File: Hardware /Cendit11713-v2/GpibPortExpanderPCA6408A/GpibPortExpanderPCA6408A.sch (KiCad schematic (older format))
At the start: 2 parts

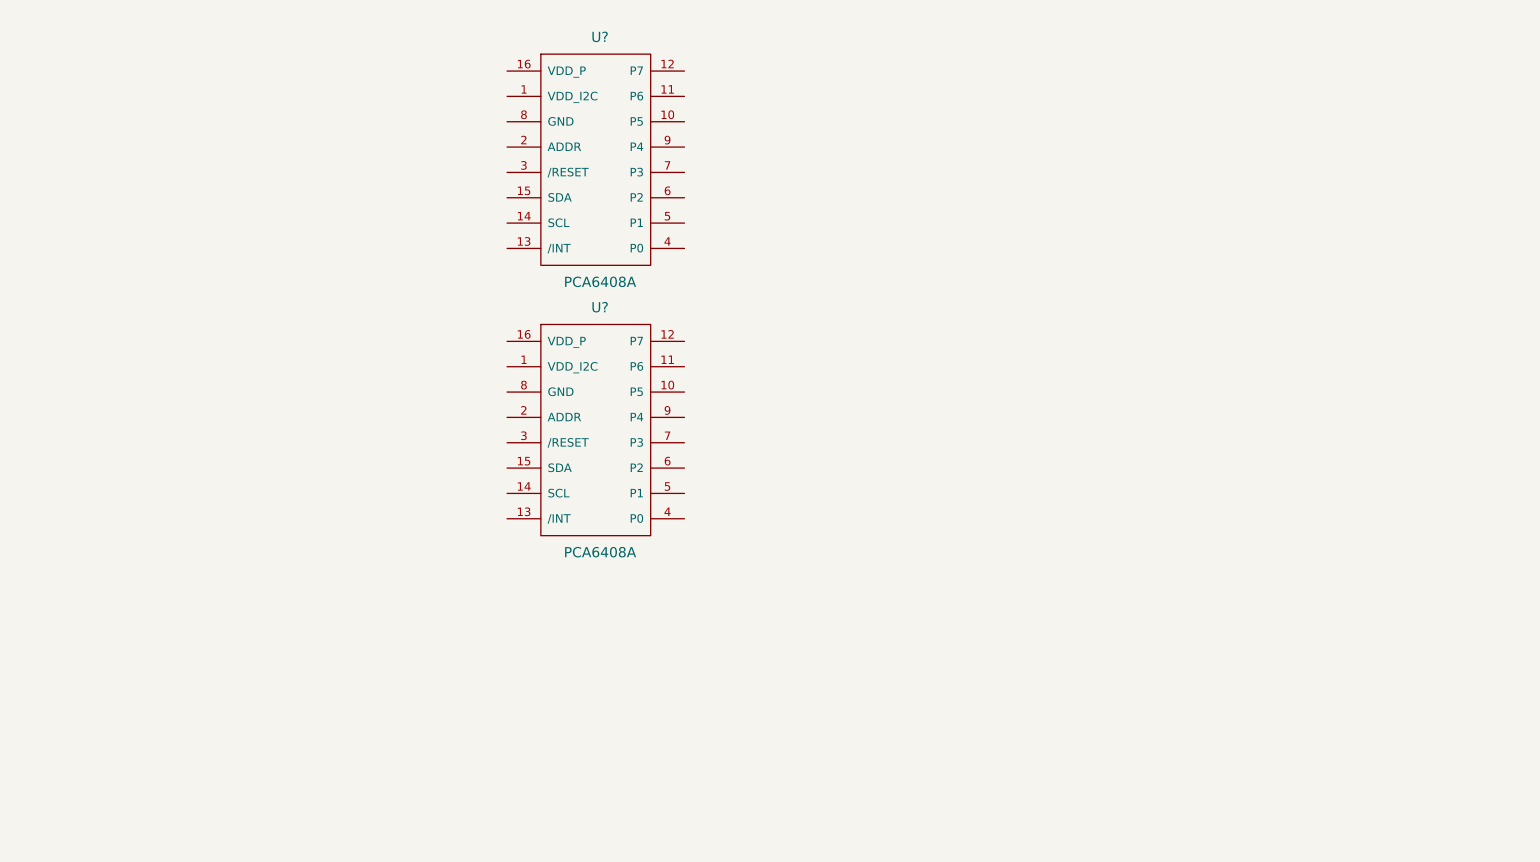
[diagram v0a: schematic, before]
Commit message: Trabajo en CenditLab.Reducido + Cendit11713
  - CenditLab componenets GUI setup frecuencia
  - Cendit11713 esquematicos expansor puerto GPIB
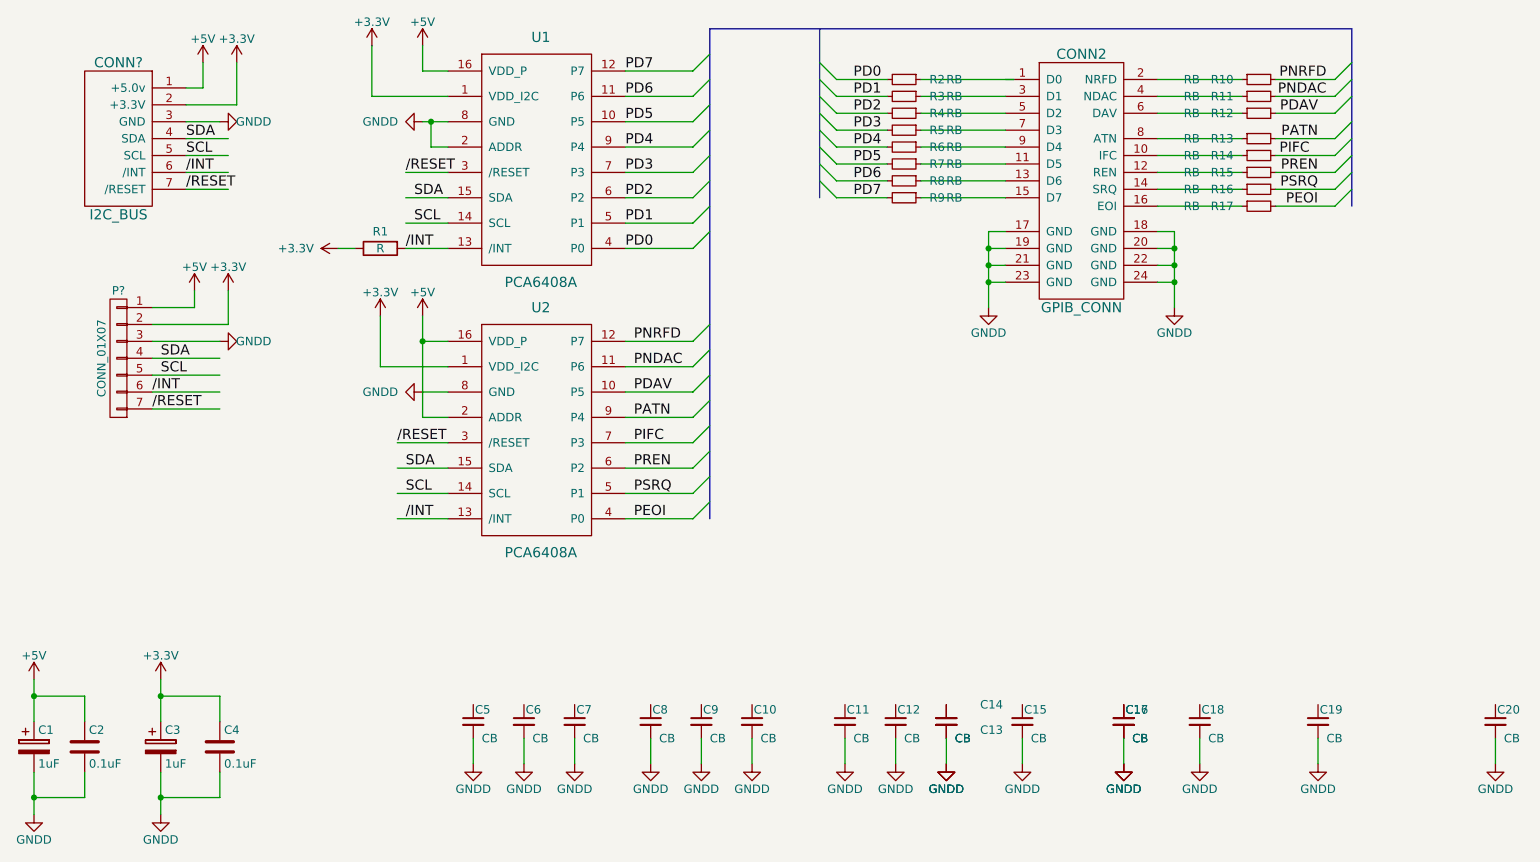
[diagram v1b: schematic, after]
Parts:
- added C1, C3: 1uF, symbol CP
- added C10, C11, C12, C13, C14, C15, C16, C17, C18, C19, C20, C5, C6, C7, C8, C9: CB, symbol C_Small
- added C2, C4: 0.1uF, symbol C
- added CONN2: GPIB_CONN, symbol GPIB_CONN
- added CONN?: I2C_BUS, symbol I2C_BUS
- added P?: CONN_01X07, symbol CONN_01X07
- added R1: R, symbol R
- added R10, R11, R12, R13, R14, R15, R16, R17, R2, R3, R4, R5, R6, R7, R8, R9: RB, symbol R_Small
- gave numbers to parts that had none: 2
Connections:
- net labels added: +3.3V, +5V, /INT, /RESET, GNDD, PATN, PD0, PD1, PD2, PD3, PD4, PD5, PD6, PD7, PDAV, PEOI, PIFC, PNDAC, PNRFD, PREN, PSRQ, SCL, SDA
- wire segments 0 -> 124
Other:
- moved on the sheet: U1, U2

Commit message: Trabajo en Cendit11713
  - Revision de esquematicos + PCBs
  - Generacion de archivos Gerber
  - CapacitiveKeyboard -> edicion PCB
  - Inicia PCB GpibPortExpander
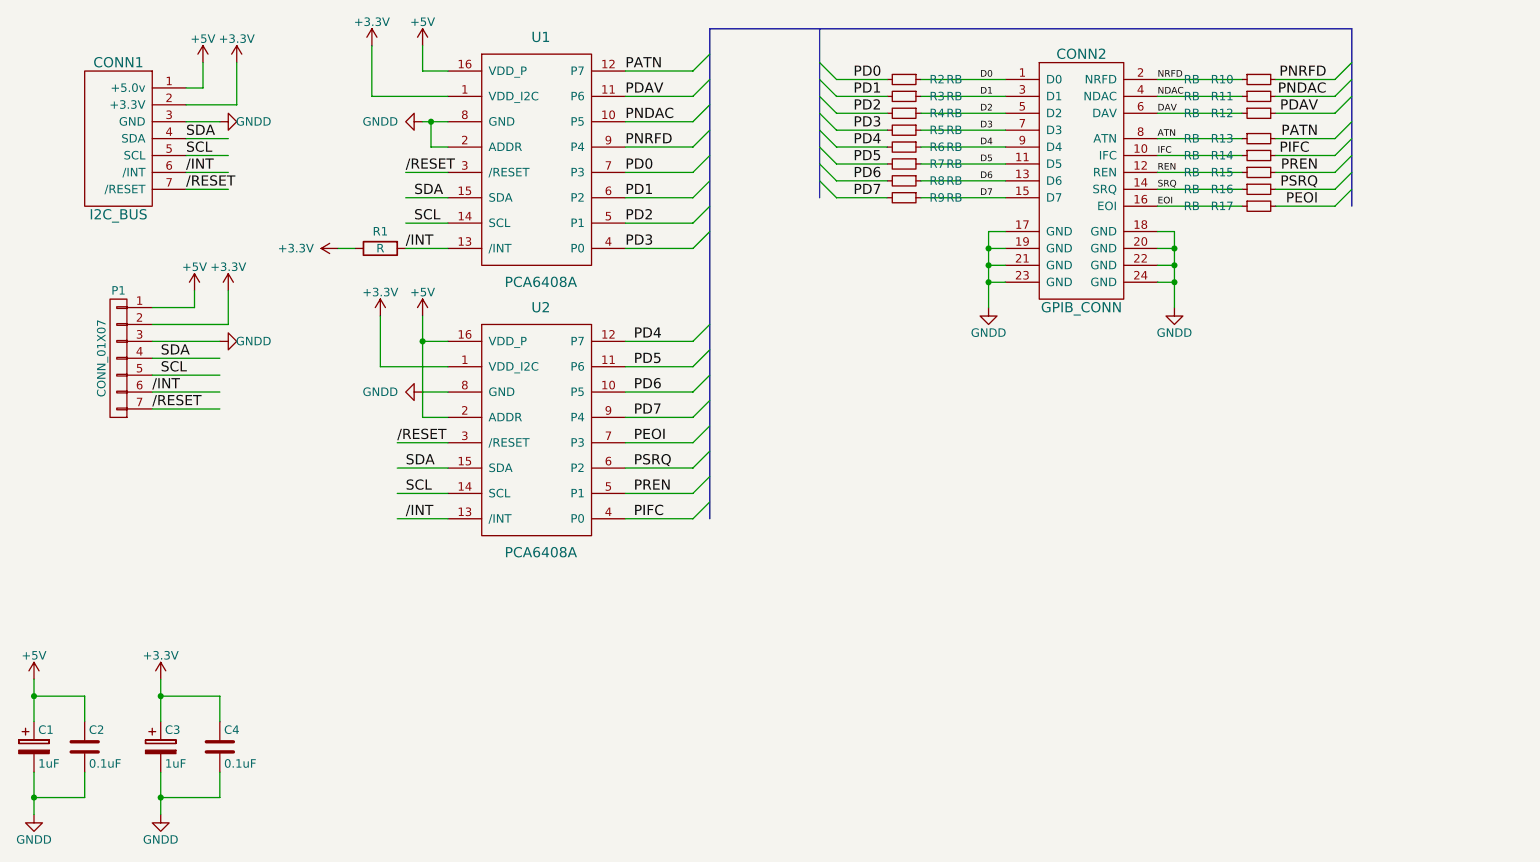
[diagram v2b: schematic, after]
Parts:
- removed C10, C11, C12, C13, C14, C15, C16, C17, C18, C19, C20, C5, C6, C7, C8, C9: CB, symbol C_Small
- C1, C3: footprint (none) -> Capacitors_SMD:C_1206_HandSoldering
- C2, C4: footprint (none) -> Capacitors_SMD:C_0805_HandSoldering
- CONN1: renamed from CONN?; footprint (none) -> CenditFootprints:SLIMLINE_SATA_PLUG_7P_6P
- CONN2: footprint (none) -> CenditFootprints:GPIB_HEADER_12X2P
- P1: renamed from P?; footprint (none) -> Pin_Headers:Pin_Header_Straight_1x07
- R1, R10, R11, R12, R13, R14, R15, R16, R17, R2, R3, R4, R5, R6, R7, R8, R9: footprint (none) -> Resistors_SMD:R_0805_HandSoldering
- U1, U2: footprint (none) -> LibreriaKicad:PCA6408A-SOP16
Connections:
- net labels added: ATN, D0, D1, D2, D3, D4, D5, D6, D7, DAV, EOI, IFC, NDAC, NRFD, REN, SRQ
- wire segments 124 -> 110

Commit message: Cendit11713 respaldo del trabajo en PCBs
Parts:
- added C5, C6, C7, C8: 0.1uF, Capacitors_SMD:C_0805_HandSoldering, symbol C_Small
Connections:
- wire segments 110 -> 118
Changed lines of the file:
@@
 	8700 2850 8800 2750
 $Comp
-L GNDD #PWR015
+L GNDD #PWR01
 U 1 1 59DB585D
 P 6650 3450
-F 0 "#PWR015" H 6650 3200 50  0001 C CNN
+F 0 "#PWR01" H 6650 3200 50  0001 C CNN
 F 1 "GNDD" H 6650 3300 50  0000 C CNN
 F 2 "" H 6650 3450 50  0000 C CNN
@@
 $EndComp
 $Comp
-L GNDD #PWR016
+L GNDD #PWR02
 U 1 1 59DB58B7
 P 7750 3450
-F 0 "#PWR016" H 7750 3200 50  0001 C CNN
+F 0 "#PWR02" H 7750 3200 50  0001 C CNN
 F 1 "GNDD" H 7750 3300 50  0000 C CNN
 F 2 "" H 7750 3450 50  0000 C CNN
@@
 	8800 1800 8800 2850
 $Comp
-L GNDD #PWR017
+L GNDD #PWR03
 U 1 1 59DBC807
 P 3300 2350
-F 0 "#PWR017" H 3300 2100 50  0001 C CNN
+F 0 "#PWR03" H 3300 2100 50  0001 C CNN
 F 1 "GNDD" V 3300 2100 50  0000 C CNN
 F 2 "" H 3300 2350 50  0000 C CNN
@@
 $EndComp
 $Comp
-L GNDD #PWR018
+L GNDD #PWR04
 U 1 1 59DBCE1F
 P 3300 3950
-F 0 "#PWR018" H 3300 3700 50  0001 C CNN
+F 0 "#PWR04" H 3300 3700 50  0001 C CNN
 F 1 "GNDD" V 3300 3700 50  0000 C CNN
 F 2 "" H 3300 3950 50  0000 C CNN
@@
 $EndComp
 $Comp
-L +5V #PWR019
+L +5V #PWR05
 U 1 1 59DBD1EE
 P 3300 1900
-F 0 "#PWR019" H 3300 1750 50  0001 C CNN
+F 0 "#PWR05" H 3300 1750 50  0001 C CNN
 F 1 "+5V" H 3300 2040 50  0000 C CNN
 F 2 "" H 3300 1900 50  0000 C CNN
@@
 $EndComp
 $Comp
-L +3.3V #PWR020
+L +3.3V #PWR06
 U 1 1 59DBD248
 P 3050 3500
-F 0 "#PWR020" H 3050 3350 50  0001 C CNN
+F 0 "#PWR06" H 3050 3350 50  0001 C CNN
 F 1 "+3.3V" H 3050 3640 50  0000 C CNN
 F 2 "" H 3050 3500 50  0000 C CNN
@@
 $EndComp
 $Comp
-L +3.3V #PWR021
+L +3.3V #PWR07
 U 1 1 59DBD2A2
 P 3000 1900
-F 0 "#PWR021" H 3000 1750 50  0001 C CNN
+F 0 "#PWR07" H 3000 1750 50  0001 C CNN
 F 1 "+3.3V" H 3000 2040 50  0000 C CNN
 F 2 "" H 3000 1900 50  0000 C CNN
@@
 $EndComp
 $Comp
-L +5V #PWR022
+L +5V #PWR08
 U 1 1 59DBD36F
 P 3300 3500
-F 0 "#PWR022" H 3300 3350 50  0001 C CNN
+F 0 "#PWR08" H 3300 3350 50  0001 C CNN
 F 1 "+5V" H 3300 3640 50  0000 C CNN
 F 2 "" H 3300 3500 50  0000 C CNN
@@
 $EndComp
 $Comp
-L +5V #PWR023
+L +5V #PWR09
 U 1 1 59DC459B
 P 1000 5650
-F 0 "#PWR023" H 1000 5500 50  0001 C CNN
+F 0 "#PWR09" H 1000 5500 50  0001 C CNN
 F 1 "+5V" H 1000 5790 50  0000 C CNN
 F 2 "" H 1000 5650 50  0000 C CNN
@@
 $EndComp
 $Comp
-L +3.3V #PWR024
+L +3.3V #PWR010
 U 1 1 59DC4624
 P 1750 5650
-F 0 "#PWR024" H 1750 5500 50  0001 C CNN
+F 0 "#PWR010" H 1750 5500 50  0001 C CNN
 F 1 "+3.3V" H 1750 5790 50  0000 C CNN
 F 2 "" H 1750 5650 50  0000 C CNN
@@
 $EndComp
 $Comp
-L GNDD #PWR025
+L GNDD #PWR011
 U 1 1 59DC46AD
 P 1000 6450
-F 0 "#PWR025" H 1000 6200 50  0001 C CNN
+F 0 "#PWR011" H 1000 6200 50  0001 C CNN
 F 1 "GNDD" H 1000 6300 50  0000 C CNN
 F 2 "" H 1000 6450 50  0000 C CNN
@@
 $EndComp
 $Comp
-L GNDD #PWR026
+L GNDD #PWR012
 U 1 1 59DC470F
 P 1750 6450
-F 0 "#PWR026" H 1750 6200 50  0001 C CNN
+F 0 "#PWR012" H 1750 6200 50  0001 C CNN
 F 1 "GNDD" H 1750 6300 50  0000 C CNN
 F 2 "" H 1750 6450 50  0000 C CNN
@@
 Connection ~ 1000 5750
 $Comp
-L +5V #PWR027
+L +5V #PWR013
 U 1 1 59DCDA03
 P 2000 2000
-F 0 "#PWR027" H 2000 1850 50  0001 C CNN
+F 0 "#PWR013" H 2000 1850 50  0001 C CNN
 F 1 "+5V" H 2000 2140 50  0000 C CNN
 F 2 "" H 2000 2000 50  0000 C CNN
@@
 $EndComp
 $Comp
-L +3.3V #PWR028
+L +3.3V #PWR014
 U 1 1 59DCDAB7
 P 2200 2000
-F 0 "#PWR028" H 2200 1850 50  0001 C CNN
+F 0 "#PWR014" H 2200 1850 50  0001 C CNN
 F 1 "+3.3V" H 2200 2140 50  0000 C CNN
 F 2 "" H 2200 2000 50  0000 C CNN
@@
 $EndComp
 $Comp
-L GNDD #PWR029
+L GNDD #PWR015
 U 1 1 59DCE1D3
 P 2100 2350
-F 0 "#PWR029" H 2100 2100 50  0001 C CNN
+F 0 "#PWR015" H 2100 2100 50  0001 C CNN
 F 1 "GNDD" V 2100 2150 50  0000 C CNN
 F 2 "" H 2100 2350 50  0000 C CNN
@@
 $EndComp
 $Comp
-L +3.3V #PWR030
+L +3.3V #PWR016
 U 1 1 59DCEC01
 P 2800 3100
-F 0 "#PWR030" H 2800 2950 50  0001 C CNN
+F 0 "#PWR016" H 2800 2950 50  0001 C CNN
 F 1 "+3.3V" V 2800 3350 50  0000 C CNN
 F 2 "" H 2800 3100 50  0000 C CNN
@@
 SDA
 $Comp
-L +5V #PWR031
+L +5V #PWR017
 U 1 1 59DDB82D
 P 1950 3350
-F 0 "#PWR031" H 1950 3200 50  0001 C CNN
+F 0 "#PWR017" H 1950 3200 50  0001 C CNN
 F 1 "+5V" H 1950 3490 50  0000 C CNN
 F 2 "" H 1950 3350 50  0000 C CNN
@@
 $EndComp
 $Comp
-L +3.3V #PWR032
+L +3.3V #PWR018
 U 1 1 59DDB90F
 P 2150 3350
-F 0 "#PWR032" H 2150 3200 50  0001 C CNN
+F 0 "#PWR018" H 2150 3200 50  0001 C CNN
 F 1 "+3.3V" H 2150 3490 50  0000 C CNN
 F 2 "" H 2150 3350 50  0000 C CNN
@@
 $EndComp
 $Comp
-L GNDD #PWR033
+L GNDD #PWR019
 U 1 1 59DDB9C4
 P 2100 3650
-F 0 "#PWR033" H 2100 3400 50  0001 C CNN
+F 0 "#PWR019" H 2100 3400 50  0001 C CNN
 F 1 "GNDD" V 2100 3450 50  0000 C CNN
 F 2 "" H 2100 3650 50  0000 C CNN
@@
 	1    0    0    -1
 $EndComp
+$Comp
+L C_Small C5
+U 1 1 59EA16DE
+P 2550 6050
+F 0 "C5" H 2560 6120 50  0000 L CNN
+F 1 "0.1uF" H 2560 5970 50  0000 L CNN
+F 2 "Capacitors_SMD:C_0805_HandSoldering" H 2550 6050 50  0001 C CNN
+F 3 "" H 2550 6050 50  0001 C CNN
+	1    2550 6050
+	1    0    0    -1
+$EndComp
+$Comp
+L C_Small C6
+U 1 1 59EA1874
+P 3000 6050
+F 0 "C6" H 3010 6120 50  0000 L CNN
+F 1 "0.1uF" H 3010 5970 50  0000 L CNN
+F 2 "Capacitors_SMD:C_0805_HandSoldering" H 3000 6050 50  0001 C CNN
+F 3 "" H 3000 6050 50  0001 C CNN
+	1    3000 6050
+	1    0    0    -1
+$EndComp
+$Comp
+L GNDD #PWR020
+U 1 1 59EA1957
+P 2550 6300
+F 0 "#PWR020" H 2550 6050 50  0001 C CNN
+F 1 "GNDD" H 2550 6150 50  0000 C CNN
+F 2 "" H 2550 6300 50  0000 C CNN
+F 3 "" H 2550 6300 50  0000 C CNN
+	1    2550 6300
+	1    0    0    -1
+$EndComp
+$Comp
+L GNDD #PWR021
+U 1 1 59EA19B6
+P 3000 6300
+F 0 "#PWR021" H 3000 6050 50  0001 C CNN
+F 1 "GNDD" H 3000 6150 50  0000 C CNN
+F 2 "" H 3000 6300 50  0000 C CNN
+F 3 "" H 3000 6300 50  0000 C CNN
+	1    3000 6300
+	1    0    0    -1
+$EndComp
+Wire Wire Line
+	2550 6150 2550 6300
+Wire Wire Line
+	3000 6150 3000 6300
+Wire Wire Line
+	2550 5950 2550 5700
+Wire Wire Line
+	3000 5950 3000 5700
+$Comp
+L +5V #PWR022
+U 1 1 59EA2054
+P 2550 5700
+F 0 "#PWR022" H 2550 5550 50  0001 C CNN
+F 1 "+5V" H 2550 5840 50  0000 C CNN
+F 2 "" H 2550 5700 50  0000 C CNN
+F 3 "" H 2550 5700 50  0000 C CNN
+	1    2550 5700
+	1    0    0    -1
+$EndComp
+$Comp
+L +3.3V #PWR023
+U 1 1 59EA20B3
+P 3000 5700
+F 0 "#PWR023" H 3000 5550 50  0001 C CNN
+F 1 "+3.3V" H 3000 5840 50  0000 C CNN
+F 2 "" H 3000 5700 50  0000 C CNN
+F 3 "" H 3000 5700 50  0000 C CNN
+	1    3000 5700
+	1    0    0    -1
+$EndComp
+$Comp
+L C_Small C7
+U 1 1 59EA218A
+P 3450 6050
+F 0 "C7" H 3460 6120 50  0000 L CNN
+F 1 "0.1uF" H 3460 5970 50  0000 L CNN
+F 2 "Capacitors_SMD:C_0805_HandSoldering" H 3450 6050 50  0001 C CNN
+F 3 "" H 3450 6050 50  0001 C CNN
+	1    3450 6050
+	1    0    0    -1
+$EndComp
+$Comp
+L C_Small C8
+U 1 1 59EA2190
+P 3900 6050
+F 0 "C8" H 3910 6120 50  0000 L CNN
+F 1 "0.1uF" H 3910 5970 50  0000 L CNN
+F 2 "Capacitors_SMD:C_0805_HandSoldering" H 3900 6050 50  0001 C CNN
+F 3 "" H 3900 6050 50  0001 C CNN
+	1    3900 6050
+	1    0    0    -1
+$EndComp
+$Comp
+L GNDD #PWR024
+U 1 1 59EA2196
+P 3450 6300
+F 0 "#PWR024" H 3450 6050 50  0001 C CNN
+F 1 "GNDD" H 3450 6150 50  0000 C CNN
+F 2 "" H 3450 6300 50  0000 C CNN
+F 3 "" H 3450 6300 50  0000 C CNN
+	1    3450 6300
+	1    0    0    -1
+$EndComp
+$Comp
+L GNDD #PWR025
+U 1 1 59EA219C
+P 3900 6300
+F 0 "#PWR025" H 3900 6050 50  0001 C CNN
+F 1 "GNDD" H 3900 6150 50  0000 C CNN
+F 2 "" H 3900 6300 50  0000 C CNN
+F 3 "" H 3900 6300 50  0000 C CNN
+	1    3900 6300
+	1    0    0    -1
+$EndComp
+Wire Wire Line
+	3450 6150 3450 6300
+Wire Wire Line
+	3900 6150 3900 6300
+Wire Wire Line
+	3450 5950 3450 5700
+Wire Wire Line
+	3900 5950 3900 5700
+$Comp
+L +5V #PWR026
+U 1 1 59EA21A6
+P 3450 5700
+F 0 "#PWR026" H 3450 5550 50  0001 C CNN
+F 1 "+5V" H 3450 5840 50  0000 C CNN
+F 2 "" H 3450 5700 50  0000 C CNN
+F 3 "" H 3450 5700 50  0000 C CNN
+	1    3450 5700
+	1    0    0    -1
+$EndComp
+$Comp
+L +3.3V #PWR027
+U 1 1 59EA21AC
+P 3900 5700
+F 0 "#PWR027" H 3900 5550 50  0001 C CNN
+F 1 "+3.3V" H 3900 5840 50  0000 C CNN
+F 2 "" H 3900 5700 50  0000 C CNN
+F 3 "" H 3900 5700 50  0000 C CNN
+	1    3900 5700
+	1    0    0    -1
+$EndComp

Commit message: En CenditLab.Reducido + respaldo de esquematicos + PCBs
  - Clases vistas para cada paso de medicion
  - Respaldo de archivos Cendit11713 (esquematicos + PCBs)
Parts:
- CONN2: symbol GPIB_CONN -> GPIB_CONN-RESCUE-GpibPortExpanderPCA6408A
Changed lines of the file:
@@
 EESchema Schematic File Version 2
+LIBS:GpibPortExpanderPCA6408A-rescue
 LIBS:adc-dac
 LIBS:memory
@@
 	6250 2100 6750 2100
 $Comp
-L GPIB_CONN CONN2
+L GPIB_CONN-RESCUE-GpibPortExpanderPCA6408A CONN2
 U 1 1 59EAE791
 P 7450 3400
